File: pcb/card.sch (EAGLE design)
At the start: 16 parts, among them IC1 74HC14D, Q1 BC817

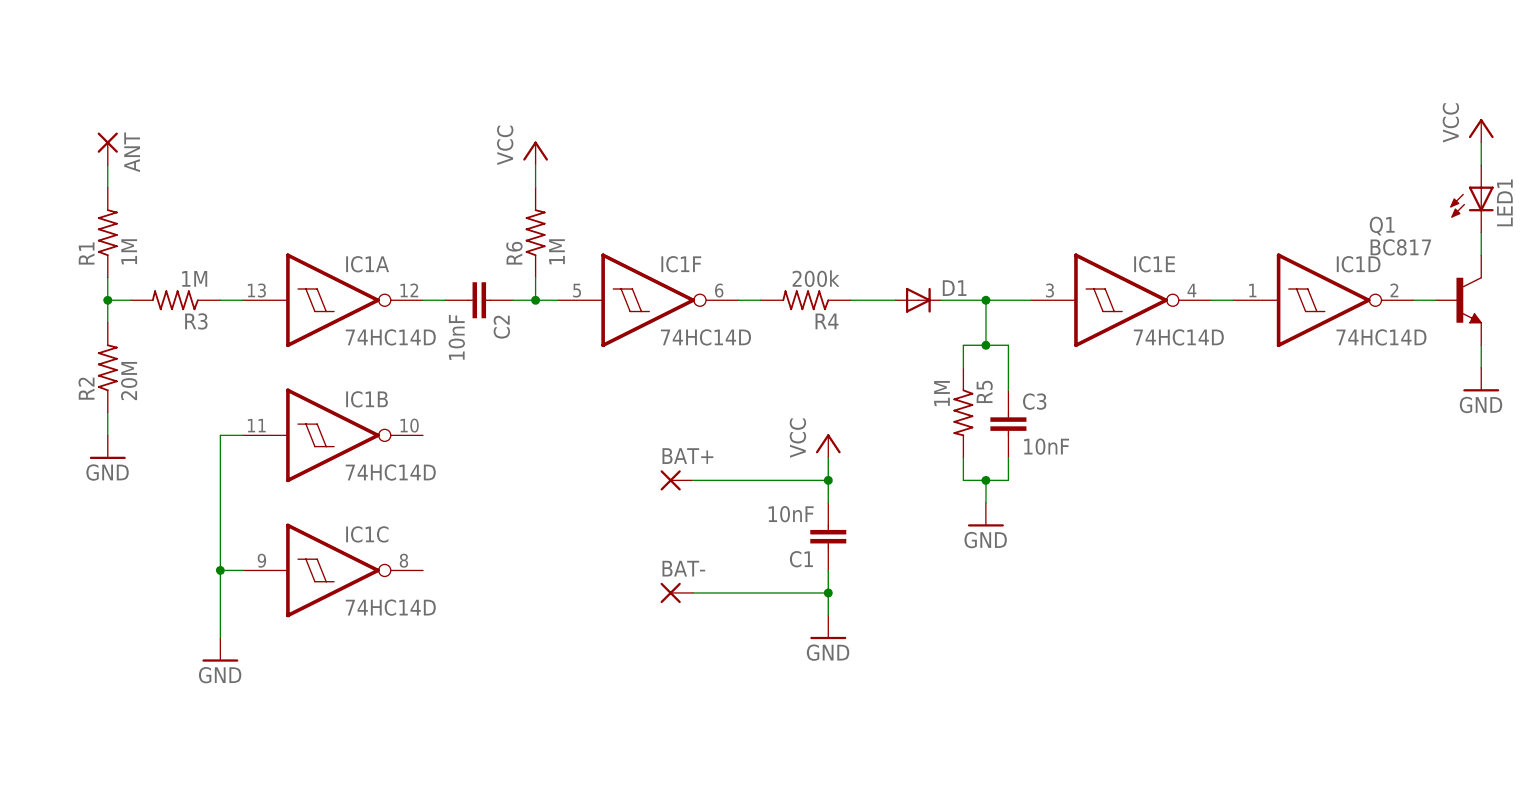
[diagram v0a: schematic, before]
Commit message: Added EEPROM for resume storage.
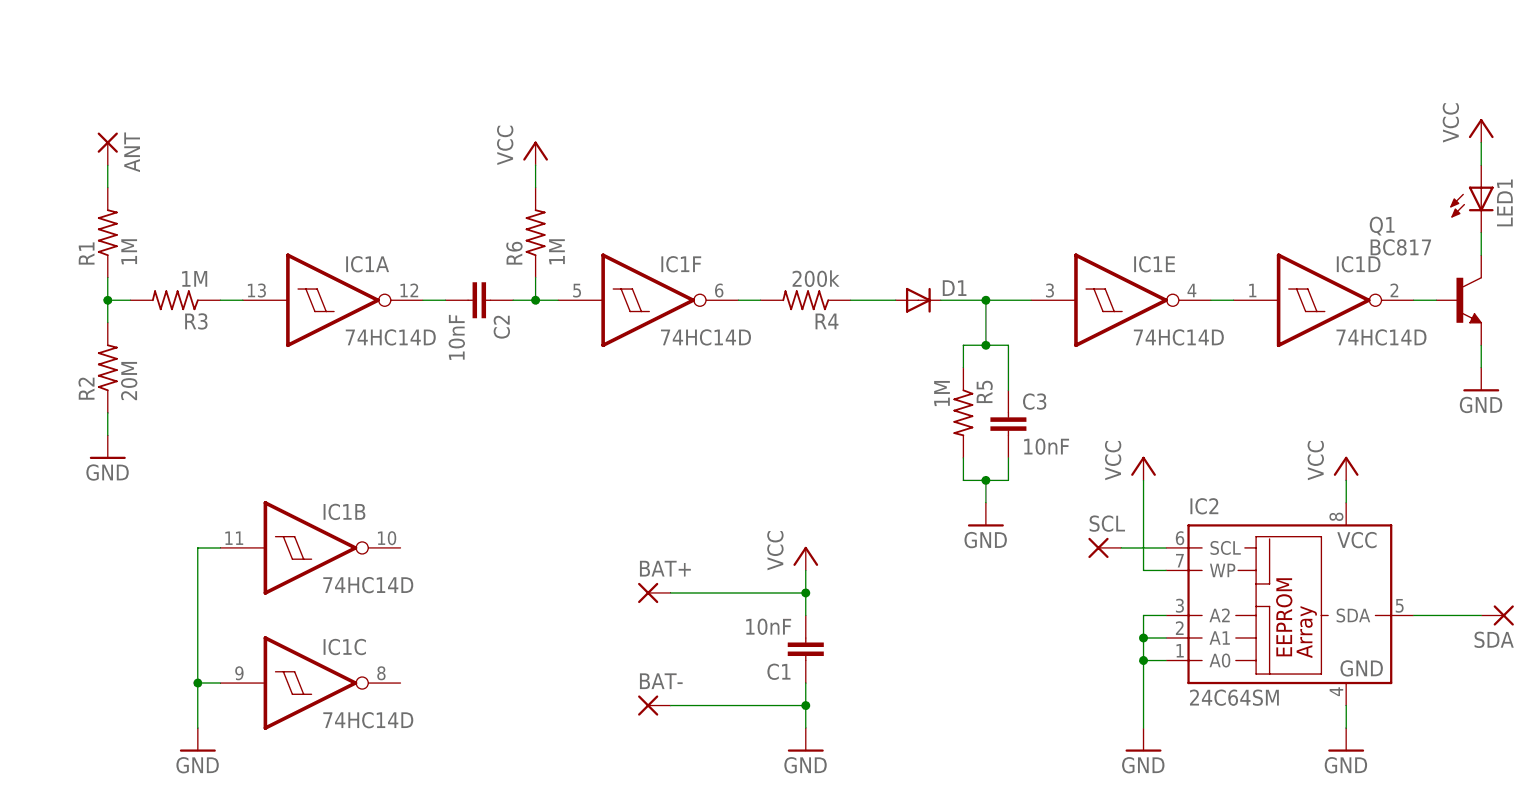
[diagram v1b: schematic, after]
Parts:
- added IC2: 24C64SM, microchip:24C64SM
- added SCL, SDA: (no value), wirepad:SMD5
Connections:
- new net N$10: IC2.SDA, SDA.P
- new net N$9: IC2.SCL, SCL.P
- net GND: now also IC2.A0, IC2.A1, IC2.A2, IC2.GND
- net VCC: now also IC2.VCC, IC2.WP
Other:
- moved on the sheet: BAT+, BAT-, C1, IC1B, IC1C
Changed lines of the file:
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@@
 <part name="BAT-" library="wirepad" deviceset="SMD5" device=""/>
 <part name="ANT" library="wirepad" deviceset="SMD5" device=""/>
+<part name="IC2" library="microchip" deviceset="24*" device="SM" technology="C64"/>
+<part name="P+4" library="supply1" deviceset="VCC" device=""/>
+<part name="GND6" library="supply1" deviceset="GND" device=""/>
+<part name="GND7" library="supply1" deviceset="GND" device=""/>
+<part name="P+5" library="supply1" deviceset="VCC" device=""/>
+<part name="SCL" library="wirepad" deviceset="SMD5" device=""/>
+<part name="SDA" library="wirepad" deviceset="SMD5" device=""/>
 </parts>
 <sheets>
@@
 </plain>
 <instances>
-<instance part="P+1" gate="VCC" x="63.5" y="35.56"/>
+<instance part="P+1" gate="VCC" x="60.96" y="22.86"/>
 <instance part="P+2" gate="VCC" x="30.48" y="68.58"/>
 <instance part="P+3" gate="VCC" x="137.16" y="71.12"/>
@@
 <instance part="R4" gate="G$1" x="60.96" y="50.8" rot="R180"/>
 <instance part="R5" gate="G$1" x="78.74" y="38.1" rot="R270"/>
-<instance part="GND1" gate="1" x="63.5" y="12.7"/>
+<instance part="GND1" gate="1" x="60.96" y="0"/>
 <instance part="GND2" gate="1" x="-17.78" y="33.02"/>
-<instance part="GND3" gate="1" x="-5.08" y="10.16"/>
+<instance part="GND3" gate="1" x="-7.62" y="0"/>
 <instance part="GND4" gate="1" x="81.28" y="25.4"/>
 <instance part="GND5" gate="1" x="137.16" y="40.64"/>
 <instance part="IC1" gate="A" x="7.62" y="50.8"/>
-<instance part="IC1" gate="B" x="7.62" y="35.56"/>
-<instance part="IC1" gate="C" x="7.62" y="20.32"/>
+<instance part="IC1" gate="B" x="5.08" y="22.86"/>
+<instance part="IC1" gate="C" x="5.08" y="7.62"/>
 <instance part="IC1" gate="D" x="119.38" y="50.8"/>
 <instance part="IC1" gate="E" x="96.52" y="50.8"/>
@@
 <instance part="LED1" gate="G$1" x="137.16" y="63.5"/>
 <instance part="R6" gate="G$1" x="30.48" y="58.42" rot="R90"/>
-<instance part="C1" gate="G$1" x="63.5" y="22.86" rot="R180"/>
+<instance part="C1" gate="G$1" x="60.96" y="10.16" rot="R180"/>
 <instance part="C2" gate="G$1" x="25.4" y="50.8" rot="R270"/>
 <instance part="C3" gate="G$1" x="83.82" y="38.1"/>
-<instance part="BAT+" gate="1" x="45.72" y="30.48"/>
-<instance part="BAT-" gate="1" x="45.72" y="17.78"/>
+<instance part="BAT+" gate="1" x="43.18" y="17.78"/>
+<instance part="BAT-" gate="1" x="43.18" y="5.08"/>
 <instance part="ANT" gate="1" x="-17.78" y="68.58" rot="R270"/>
+<instance part="IC2" gate="G$1" x="114.3" y="15.24"/>
+<instance part="P+4" gate="VCC" x="121.92" y="33.02"/>
+<instance part="GND6" gate="1" x="121.92" y="0"/>
+<instance part="GND7" gate="1" x="99.06" y="0"/>
+<instance part="P+5" gate="VCC" x="99.06" y="33.02"/>
+<instance part="SCL" gate="1" x="93.98" y="22.86"/>
+<instance part="SDA" gate="1" x="139.7" y="15.24" rot="R180"/>
 </instances>
 <busses>
@@
 <pinref part="IC1" gate="B" pin="I"/>
 <pinref part="GND3" gate="1" pin="GND"/>
-<wire x1="-2.54" y1="35.56" x2="-5.08" y2="35.56" width="0.1524" layer="91"/>
-<wire x1="-5.08" y1="35.56" x2="-5.08" y2="20.32" width="0.1524" layer="91"/>
+<wire x1="-5.08" y1="22.86" x2="-7.62" y2="22.86" width="0.1524" layer="91"/>
+<wire x1="-7.62" y1="22.86" x2="-7.62" y2="7.62" width="0.1524" layer="91"/>
 <pinref part="IC1" gate="C" pin="I"/>
-<wire x1="-5.08" y1="20.32" x2="-5.08" y2="12.7" width="0.1524" layer="91"/>
-<wire x1="-2.54" y1="20.32" x2="-5.08" y2="20.32" width="0.1524" layer="91"/>
-<junction x="-5.08" y="20.32"/>
+<wire x1="-7.62" y1="7.62" x2="-7.62" y2="2.54" width="0.1524" layer="91"/>
+<wire x1="-5.08" y1="7.62" x2="-7.62" y2="7.62" width="0.1524" layer="91"/>
+<junction x="-7.62" y="7.62"/>
 </segment>
 <segment>
@@
 <pinref part="C1" gate="G$1" pin="1"/>
 <pinref part="GND1" gate="1" pin="GND"/>
-<wire x1="63.5" y1="20.32" x2="63.5" y2="17.78" width="0.1524" layer="91"/>
+<wire x1="60.96" y1="7.62" x2="60.96" y2="5.08" width="0.1524" layer="91"/>
 <pinref part="BAT-" gate="1" pin="P"/>
-<wire x1="63.5" y1="17.78" x2="63.5" y2="15.24" width="0.1524" layer="91"/>
-<wire x1="48.26" y1="17.78" x2="63.5" y2="17.78" width="0.1524" layer="91"/>
-<junction x="63.5" y="17.78"/>
+<wire x1="60.96" y1="5.08" x2="60.96" y2="2.54" width="0.1524" layer="91"/>
+<wire x1="45.72" y1="5.08" x2="60.96" y2="5.08" width="0.1524" layer="91"/>
+<junction x="60.96" y="5.08"/>
+</segment>
+<segment>
+<pinref part="GND6" gate="1" pin="GND"/>
+<pinref part="IC2" gate="G$1" pin="GND"/>
+<wire x1="121.92" y1="2.54" x2="121.92" y2="5.08" width="0.1524" layer="91"/>
+</segment>
+<segment>
+<pinref part="IC2" gate="G$1" pin="A2"/>
+<pinref part="GND7" gate="1" pin="GND"/>
+<wire x1="101.6" y1="15.24" x2="99.06" y2="15.24" width="0.1524" layer="91"/>
+<wire x1="99.06" y1="15.24" x2="99.06" y2="12.7" width="0.1524" layer="91"/>
+<pinref part="IC2" gate="G$1" pin="A1"/>
+<wire x1="99.06" y1="12.7" x2="99.06" y2="10.16" width="0.1524" layer="91"/>
+<wire x1="99.06" y1="10.16" x2="99.06" y2="2.54" width="0.1524" layer="91"/>
+<wire x1="101.6" y1="12.7" x2="99.06" y2="12.7" width="0.1524" layer="91"/>
+<pinref part="IC2" gate="G$1" pin="A0"/>
+<wire x1="101.6" y1="10.16" x2="99.06" y2="10.16" width="0.1524" layer="91"/>
+<junction x="99.06" y="12.7"/>
+<junction x="99.06" y="10.16"/>
 </segment>
 </net>
@@
 <pinref part="P+1" gate="VCC" pin="VCC"/>
 <pinref part="C1" gate="G$1" pin="2"/>
-<wire x1="63.5" y1="33.02" x2="63.5" y2="30.48" width="0.1524" layer="91"/>
+<wire x1="60.96" y1="20.32" x2="60.96" y2="17.78" width="0.1524" layer="91"/>
 <pinref part="BAT+" gate="1" pin="P"/>
-<wire x1="63.5" y1="30.48" x2="63.5" y2="27.94" width="0.1524" layer="91"/>
-<wire x1="48.26" y1="30.48" x2="63.5" y2="30.48" width="0.1524" layer="91"/>
-<junction x="63.5" y="30.48"/>
+<wire x1="60.96" y1="17.78" x2="60.96" y2="15.24" width="0.1524" layer="91"/>
+<wire x1="45.72" y1="17.78" x2="60.96" y2="17.78" width="0.1524" layer="91"/>
+<junction x="60.96" y="17.78"/>
+</segment>
+<segment>
+<pinref part="P+4" gate="VCC" pin="VCC"/>
+<pinref part="IC2" gate="G$1" pin="VCC"/>
+<wire x1="121.92" y1="30.48" x2="121.92" y2="27.94" width="0.1524" layer="91"/>
+</segment>
+<segment>
+<pinref part="IC2" gate="G$1" pin="WP"/>
+<pinref part="P+5" gate="VCC" pin="VCC"/>
+<wire x1="101.6" y1="20.32" x2="99.06" y2="20.32" width="0.1524" layer="91"/>
+<wire x1="99.06" y1="20.32" x2="99.06" y2="30.48" width="0.1524" layer="91"/>
 </segment>
 </net>
@@
 </segment>
 </net>
+<net name="N$9" class="0">
+<segment>
+<pinref part="IC2" gate="G$1" pin="SCL"/>
+<wire x1="101.6" y1="22.86" x2="96.52" y2="22.86" width="0.1524" layer="91"/>
+<pinref part="SCL" gate="1" pin="P"/>
+</segment>
+</net>
+<net name="N$10" class="0">
+<segment>
+<pinref part="IC2" gate="G$1" pin="SDA"/>
+<wire x1="137.16" y1="15.24" x2="129.54" y2="15.24" width="0.1524" layer="91"/>
+<pinref part="SDA" gate="1" pin="P"/>
+</segment>
+</net>

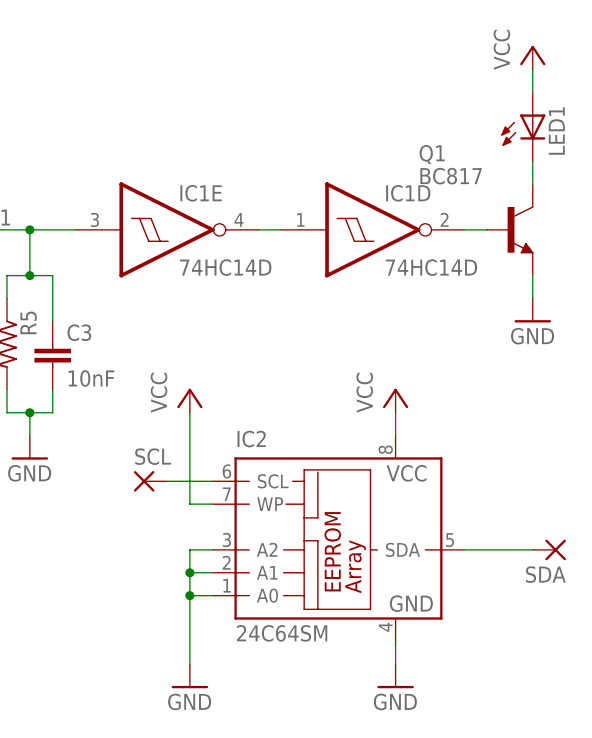
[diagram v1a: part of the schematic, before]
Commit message: Added the PCB layout.
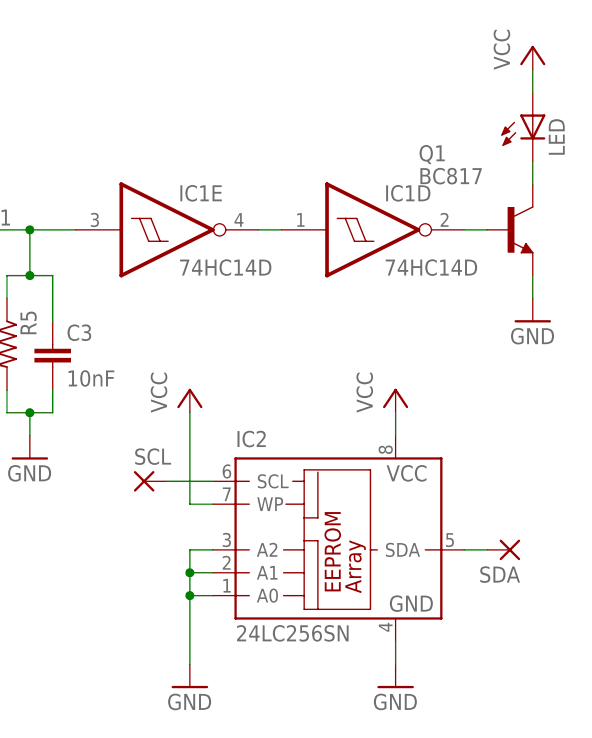
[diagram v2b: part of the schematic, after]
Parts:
- ANT, BAT+, BAT-, SCL, SDA: device wirepad:SMD5 -> wirepad:SMD2
- D1: device diode:DIODE-MELF-MLL41 -> diode:DIODE-MINIMELF
- IC2: value 24C64SM -> 24LC256SN; device microchip:24C64SM -> microchip:24LC256SN
- R1, R2, R3, R4, R5, R6: device resistor:R-US_M0805 -> resistor:R-US_M1206
- renumbered LED1 to LED
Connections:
- net N$1 renamed ANT
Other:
- moved on the sheet: SDA

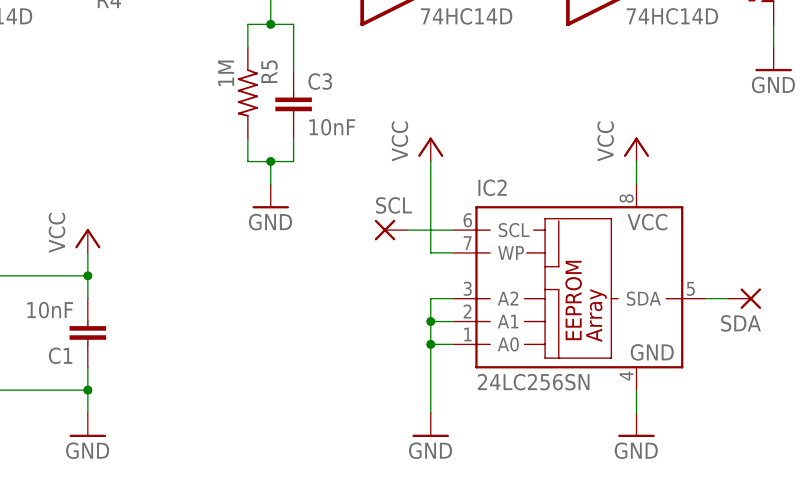
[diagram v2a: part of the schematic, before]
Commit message: Added a GND pad for the EEPROM chip.
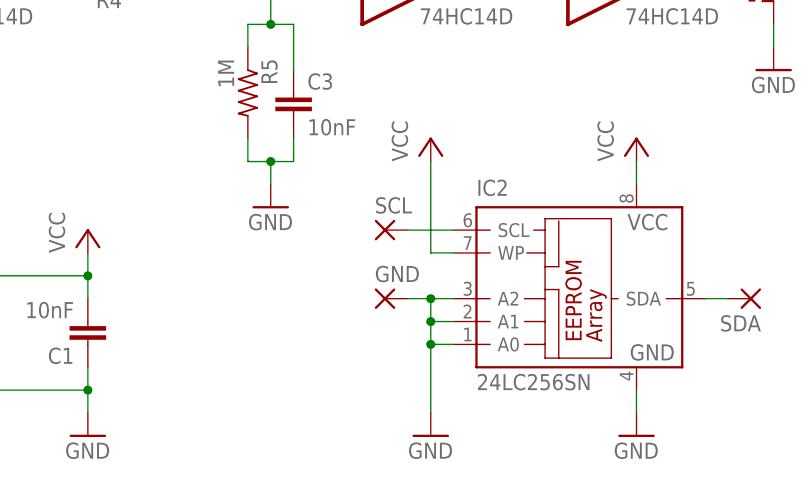
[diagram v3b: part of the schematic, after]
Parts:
- added GND: (no value), wirepad:SMD2
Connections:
- net GND: now also GND.P
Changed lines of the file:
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@@
 <part name="ANT" library="wirepad" deviceset="SMD2" device=""/>
 <part name="IC2" library="microchip" deviceset="24*" device="SN" technology="LC256"/>
+<part name="GND" library="wirepad" deviceset="SMD2" device=""/>
 </parts>
 <sheets>
@@
 <instance part="ANT" gate="1" x="-17.78" y="68.58" rot="R270"/>
 <instance part="IC2" gate="G$1" x="114.3" y="15.24"/>
+<instance part="GND" gate="1" x="93.98" y="15.24"/>
 </instances>
 <busses>
@@
 <pinref part="IC2" gate="G$1" pin="A1"/>
 <pinref part="IC2" gate="G$1" pin="A2"/>
+<pinref part="GND" gate="1" pin="P"/>
+<wire x1="99.06" y1="15.24" x2="96.52" y2="15.24" width="0.1524" layer="91"/>
+<junction x="99.06" y="15.24"/>
 </segment>
 <segment>
